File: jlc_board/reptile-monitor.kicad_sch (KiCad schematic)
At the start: 30 parts, among them IC1 ESP32-WROVER-E_M213EH6464PH3Q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, J1 UART, J2 AC_IN, J3 Conn_01x08, J7 LOAD1, J8 LOAD2, K1 ALDP105W, K2 ALDP105W, SW1 RST, SW2 BOOT, U1 NUD3105DMT1G, U3 AP2112K-3.3, Y1 32.768KHz 12.5p

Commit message: rev 2
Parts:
- removed IC1: ESP32-WROVER-E_M213EH6464PH3Q0_, SamacSys_Parts:ESP32WROVEREM213EH6464PH3Q0, symbol SamacSys_Parts:ESP32-WROVER-E_M213EH6464PH3Q0_
- removed J3: Conn_01x08, Connector_PinHeader_2.54mm:PinHeader_2x06_P2.54mm_Vertical, symbol Connector_Generic:Conn_02x06_Odd_Even
- added FB1: 360 m, Capacitor_SMD:C_0805_2012Metric, symbol Device:FerriteBead_Small
- added J1: 1-WIRE, Connector_JST:JST_SH_SM03B-SRSS-TB_1x03-1MP_P1.00mm_Horizontal, symbol Connector:Conn_01x03_Male
- added J8: I2C, Connector_JST:JST_SH_SM04B-SRSS-TB_1x04-1MP_P1.00mm_Horizontal, symbol Connector:Conn_01x04_Male
- added MD1: ESP32-WROVER-E, reptile-monitor:Espressif_Systems-ESP32-WROVER-0-0-MFG, symbol Reptile_Monitor:ESP32-WROVER-E
- added R5, R6, R7: 4.7k, Resistor_SMD:R_0603_1608Metric, symbol Device:R_Small
- U1: renamed from U3; value AP2112K-3.3 -> AP2112M-3.3
- renumbered C9 to C3, C7 to C4, C8 to C5, C10 to C6, D2 to D1, D1 to D2, J1 to J2, J2 to J3, J7 to J4, J8 to J5, R12 to R1, R13 to R2, R1 to R3, R8 to R4, U1 to U2
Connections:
- net +3V3: now also J1.3 (Pin_3), J8.1 (Pin_1), MD1.2 (VDD33), R5.1, R6.1, R7.1
- net +5V: now also FB1.1; no longer C1.1, R1.2, U1.8 (VIN)
- net EN: now also MD1.3 (EN)
- net GND: now also J1.1 (Pin_1), J8.4 (Pin_4), MD1.1 (GND), MD1.15 (GND), MD1.38 (GND), MD1.39 (GND)
- net IO0: now also MD1.25 (IO0)
- net IO18: now also MD1.30 (IO18)
- net IO19: now also MD1.31 (IO19)
- net IO21: now also MD1.33 (IO21)
- net IO22: now also MD1.36 (IO22)
- net IO23: now also MD1.37 (IO23)
- net IO25: now also J8.3 (Pin_3), MD1.10 (IO25), R5.2
- net IO26: now also J8.2 (Pin_2), MD1.11 (IO26), R6.2
- net IO27: now also J1.2 (Pin_2), MD1.12 (IO27), R7.2
- net IO36: now also MD1.4 (IO36)
- net IO39: now also MD1.5 (IO39)
- net IO5: now also MD1.29 (IO5)
- net RXD0: now also MD1.34 (RXD0)
- net TXD0: now also MD1.35 (TXD0)
- net at CL1.1, Y1.2: now also MD1.8 (IO32)
- net at CL2.1, Y1.1: now also MD1.9 (IO33)
- net IO12 renamed MISO
- net MISO: now also MD1.14 (IO12)
- net IO13 renamed LED
- net LED: now also MD1.24 (IO2)
- net IO14 renamed SCLK
- net SCLK: now also MD1.13 (IO14)
- new net: C1.1, FB1.2, R1.2, U1.8 (VIN)
- new net CS0: MD1.23 (IO15)
- new net IO34: MD1.6 (IO34)
- new net IO35: MD1.7 (IO35)
- new net IO4: MD1.26 (IO4)
- new net MOSI: MD1.16 (IO13)
- no-connect marks 10 -> 3
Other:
- note added: "Connectors"
- note removed: "IO Pin Headers"
- moved on the sheet: C4, C5, CL1, CL2, D2, J2, R4, Y1

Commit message: Rev2 - Waffle & Wesley
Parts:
- removed J3: AC_IN, reptile-monitor:Molex-43650-0215-0-0-MFG, symbol Reptile_Monitor:43650-0215
- removed J4: LOAD1, reptile-monitor:Molex-43650-0215-0-0-MFG, symbol Reptile_Monitor:43650-0215
- removed J5: LOAD2, reptile-monitor:Molex-43650-0215-0-0-MFG, symbol Reptile_Monitor:43650-0215
- added J3: AC_IN, SamacSys_Parts:128340212, symbol Connector:Screw_Terminal_01x02
- added J4: LOAD_1, SamacSys_Parts:128340212, symbol Connector:Screw_Terminal_01x02
- added J5: LOAD_2, SamacSys_Parts:128340212, symbol Connector:Screw_Terminal_01x02
- added J6: I/O, Connector_PinHeader_1.27mm:PinHeader_2x05_P1.27mm_Vertical_SMD, symbol Connector_Generic:Conn_02x05_Odd_Even
- C1, C2: footprint Capacitor_SMD:C_0805_2012Metric -> Capacitor_SMD:C_0603_1608Metric
- FB1: footprint Capacitor_SMD:C_0805_2012Metric -> Inductor_SMD:L_0805_2012Metric
- SW1: value RST -> RESET
- renumbered R6 to R5, R5 to R6
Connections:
- net +3V3: now also J6.1 (Pin_1), J6.10 (Pin_10)
- net AC_L: now also F1.2, J3.1 (Pin_1); no longer F1.1
- net AC_N: now also J3.2 (Pin_2), J4.1 (Pin_1), J5.1 (Pin_1)
- net CS0: now also J6.8 (Pin_8)
- net FUSED_AC_L: now also F1.1; no longer F1.2
- net GND: now also J6.9 (Pin_9)
- net IO25: now also J6.7 (Pin_7); no longer J8.3 (Pin_3), R6.2
- net IO26: now also J6.5 (Pin_5); no longer J8.2 (Pin_2), R5.2
- net IO27: now also J6.3 (Pin_3); no longer J1.2 (Pin_2), R7.2
- net LOAD1: now also J4.2 (Pin_2)
- net LOAD2: now also J5.2 (Pin_2)
- net IO0 renamed BOOT
- net IO18 renamed 1-WIRE
- net 1-WIRE: now also J1.2 (Pin_2), R7.2
- net IO19 renamed L1
- net L1: now also U2.2 (1_Gate)
- net IO21 renamed L2
- net L2: now also U2.5 (2_Gate)
- net IO34: no longer names the net of MD1.6 (IO34)
- net IO35: no longer names the net of MD1.7 (IO35)
- net IO4 renamed SCL
- net SCL: now also J8.3 (Pin_3), R6.2
- net IO5 renamed SDA
- net SDA: now also J8.2 (Pin_2), R5.2
- net MISO renamed SDI
- net SDI: now also J6.2 (Pin_2); no longer U2.5 (2_Gate)
- net MOSI renamed SDO
- net SDO: now also J6.4 (Pin_4)
- net SCLK renamed SCK
- net SCK: now also J6.6 (Pin_6); no longer U2.2 (1_Gate)
- no-connect marks 3 -> 7
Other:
- moved on the sheet: C1, C2, D1, F1, FB1, J1, J2, J8, PS1, R1, R2, R5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

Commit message: Revision 3
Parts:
- removed CL1, CL2: 20p, Capacitor_SMD:C_0603_1608Metric, symbol Device:C_Small
- removed SW1: RESET, reptile-monitor:Omron-B3U-1000P-MFG, symbol Reptile_Monitor:B3U-1000P
- removed SW2: BOOT, reptile-monitor:Omron-B3U-1000P-MFG, symbol Reptile_Monitor:B3U-1000P
- removed Y1: 32.768KHz 12.5p, reptile-monitor:Crystal_SMD_3215-2Pin_3.2x1.5mm, symbol Device:Crystal_Small
- added C7: 100n, Capacitor_SMD:C_0603_1608Metric, symbol Device:C_Small
- added D3: Schottky, Diode_SMD:D_SOD-523, symbol Device:D_Schottky_Small
- added SW1: RESET, reptile-monitor:CK-KMR221GLFS-MFG, symbol Reptile_Monitor:KMR221GLFS
- added SW2: BOOT, reptile-monitor:CK-KMR221GLFS-MFG, symbol Reptile_Monitor:KMR221GLFS
- C3, C6: value 0.1u -> 100n
- C4: value 0.1u -> 22u
- C5: value 22u -> 100n
- D1: value LED -> RED
- D2: value LED -> BLUE
- FB1: footprint Inductor_SMD:L_0805_2012Metric -> Inductor_SMD:L_0603_1608Metric_Pad1.05x0.95mm_HandSolder
- R2, R4: value 100r -> 10k
- R3: LCSC (none) -> C22775
- R5, R6, R7: value 4.7k -> 10k
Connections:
- net +3V3: now also R3.2; no longer J2.1 (Pin_1), J6.1 (Pin_1)
- net +5V: now also D3.1 (K)
- net BOOT: now also SW2.1, SW2.2
- net CS0: now also MD1.12 (IO27); no longer MD1.23 (IO15)
- net EN: now also C3.1, C7.1, SW1.1, SW1.2
- net GND: now also D2.1 (K), J2.1 (Pin_1), C7.2, SW1.3, SW1.4, SW1.5 (GROUND), SW2.3, SW2.4, SW2.5 (GROUND); no longer J2.4 (Pin_4), R4.2
- net IO25: now also J6.3 (Pin_3); no longer J6.7 (Pin_7)
- net IO26: now also J6.1 (Pin_1); no longer J6.5 (Pin_5)
- net LED: now also MD1.23 (IO15), R4.2; no longer D2.1 (K), MD1.24 (IO2)
- net RXD0: now also J2.3 (Pin_3); no longer J2.2 (Pin_2)
- net TXD0: now also J2.2 (Pin_2); no longer J2.3 (Pin_3)
- net IO34: now reaches MD1.6 (IO34)
- net IO34: now also J6.7 (Pin_7)
- net IO35: now reaches MD1.7 (IO35)
- net IO35: now also J6.5 (Pin_5)
- net IO22: no longer names the net of MD1.36 (IO22)
- net IO23: no longer names the net of MD1.37 (IO23)
- removed net IO27: J6.3 (Pin_3), MD1.12 (IO27)
- net IO36: no longer names the net of MD1.4 (IO36)
- net IO39: no longer names the net of MD1.5 (IO39)
- new net: D3.2 (A), J2.4 (Pin_4)
- new net IO2: MD1.24 (IO2)
- no-connect marks 7 -> 10
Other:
- moved on the sheet: C4, C5, C6, D2, R4

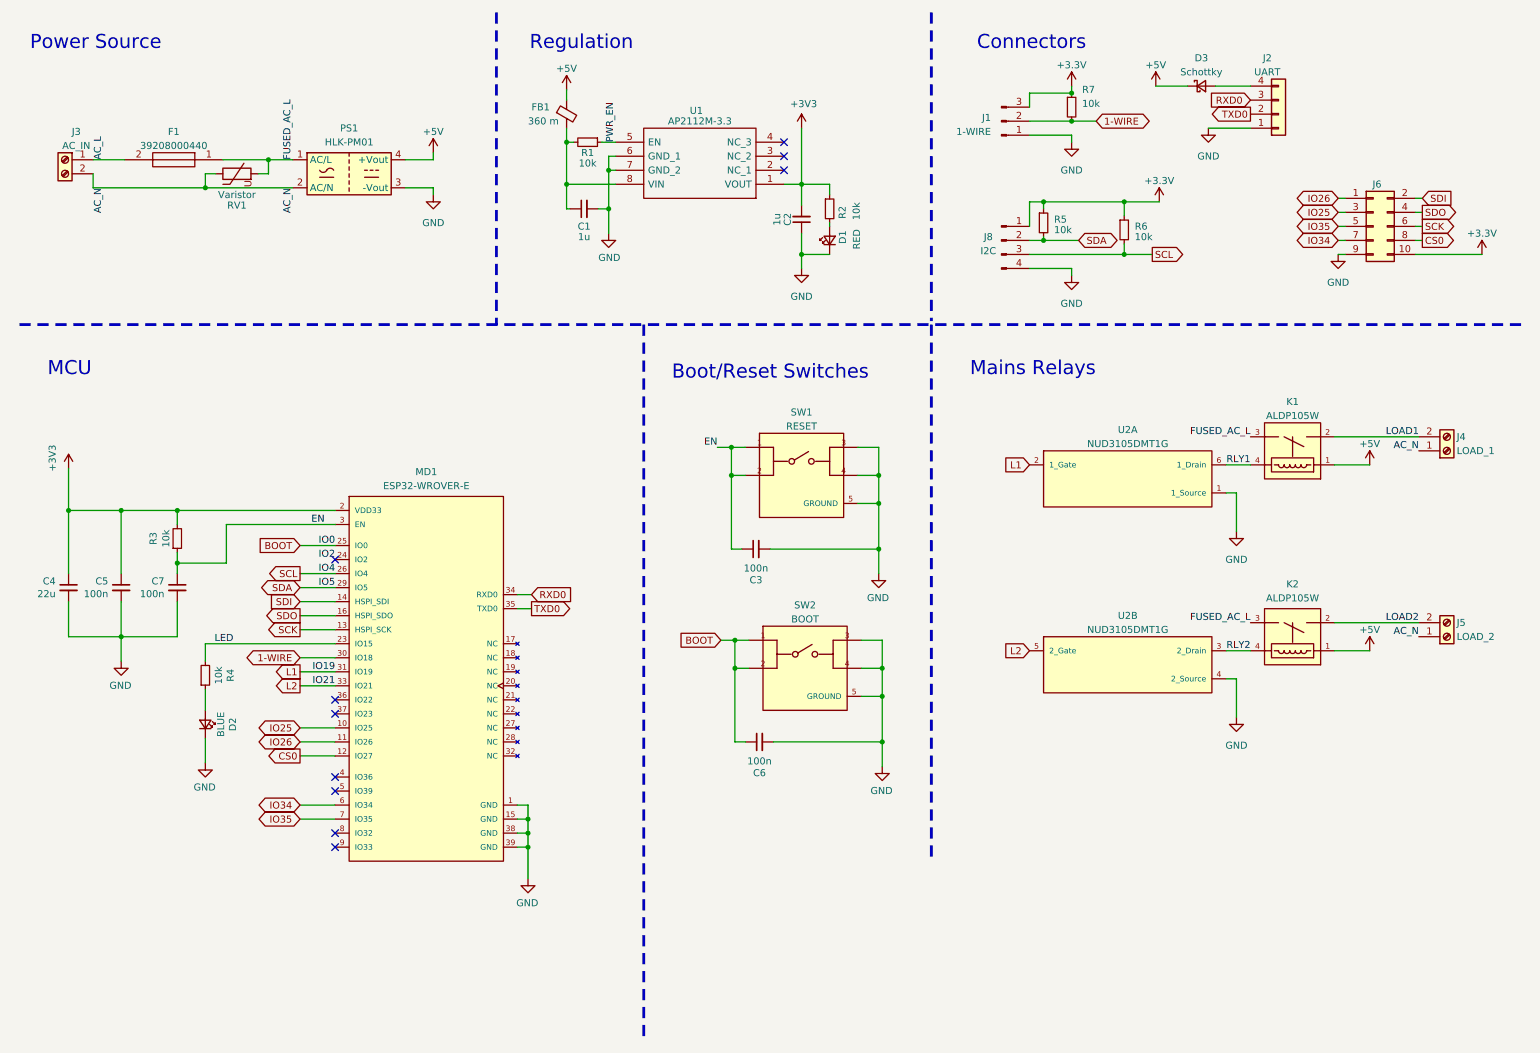
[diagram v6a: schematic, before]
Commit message: separate power board
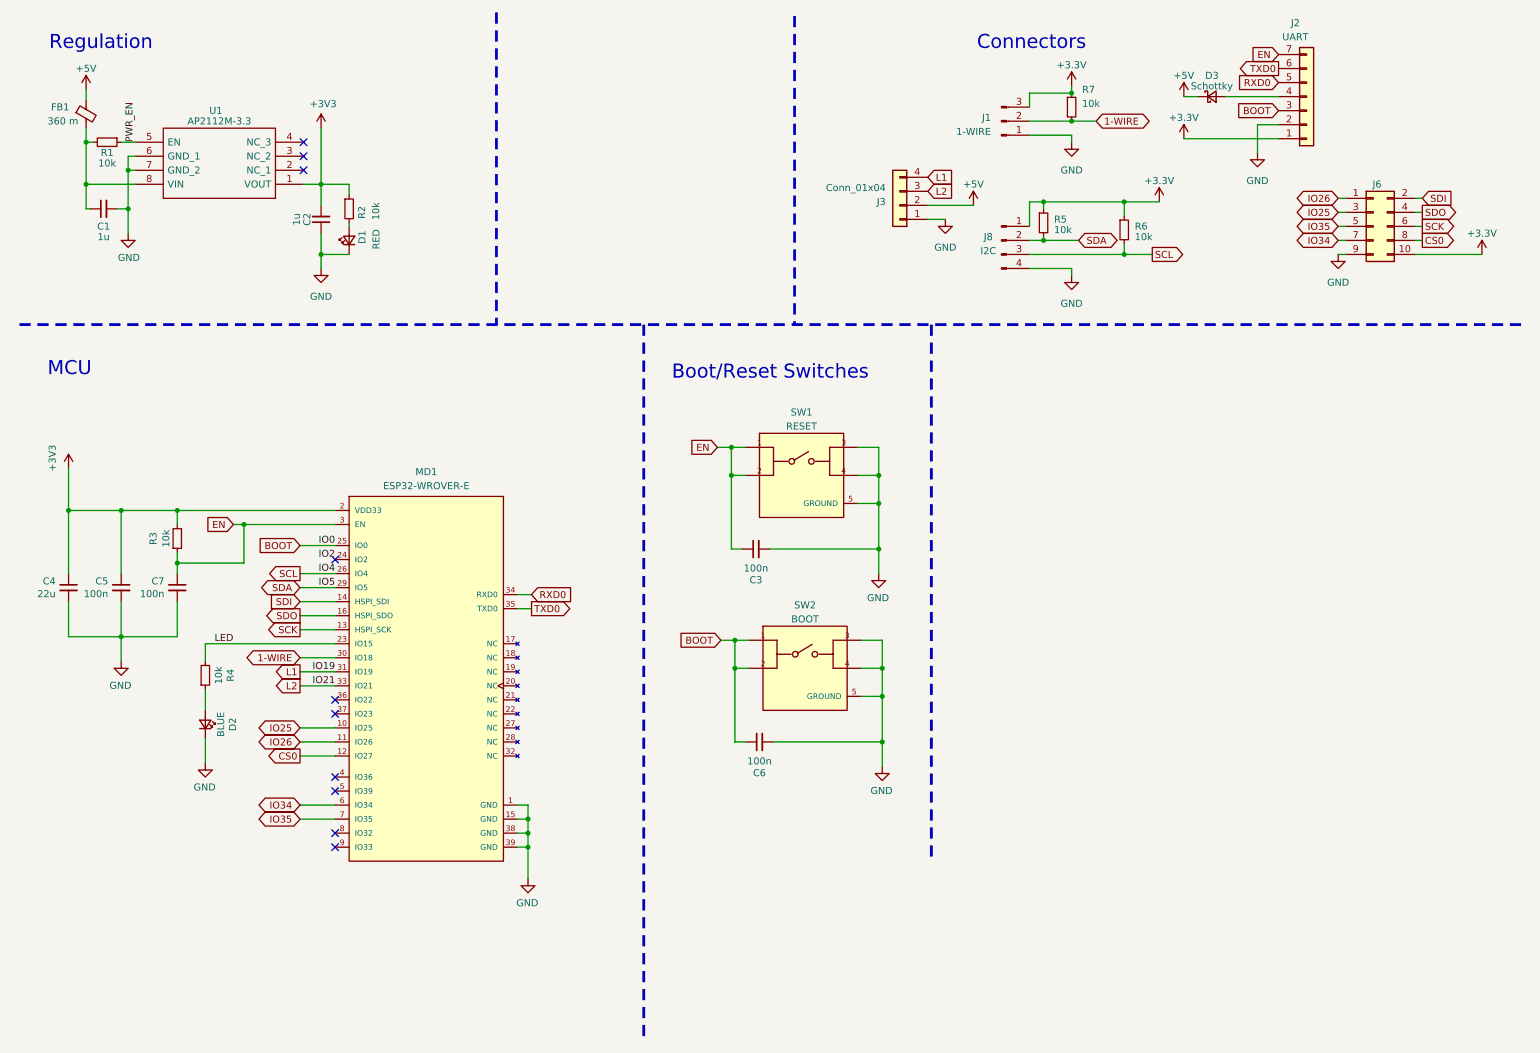
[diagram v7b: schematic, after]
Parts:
- removed F1: 39208000440, SamacSys_Parts:TO508P400X850X850-2P, symbol SamacSys_Parts:39215000000
- removed J3: AC_IN, SamacSys_Parts:128340212, symbol Connector:Screw_Terminal_01x02
- removed J4: LOAD_1, SamacSys_Parts:128340212, symbol Connector:Screw_Terminal_01x02
- removed J5: LOAD_2, SamacSys_Parts:128340212, symbol Connector:Screw_Terminal_01x02
- removed K1, K2: ALDP105W, reptile-monitor:Panasonic-ALDP105W-Manufacturer_Recommended, symbol Reptile_Monitor:ALDP105W
- removed PS1: HLK-PM01, Converter_ACDC:Converter_ACDC_HiLink_HLK-PMxx, symbol Converter_ACDC:HLK-PM01
- removed RV1: Varistor, Varistor:RV_Disc_D7mm_W3.4mm_P5mm, symbol Device:Varistor
- removed U2: NUD3105DMT1G, reptile-monitor:ON_Semi-318F-0-0-0, symbol Reptile_Monitor:NUD3105DMT1G
- added J3: Conn_01x04, Connector_PinSocket_2.54mm:PinSocket_1x04_P2.54mm_Vertical, symbol Connector_Generic:Conn_01x04
- J2: footprint Connector_PinHeader_2.54mm:PinHeader_1x04_P2.54mm_Vertical -> Connector_PinHeader_2.54mm:PinHeader_1x07_P2.54mm_Vertical; symbol Connector_Generic:Conn_01x04 -> Connector_Generic:Conn_01x07
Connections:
- net +3V3: now also J2.1 (Pin_1)
- net +5V: now also J3.2 (Pin_2)
- net BOOT: now also J2.3 (Pin_3)
- net EN: now also J2.7 (Pin_7)
- net GND: now also J2.2 (Pin_2), J3.1 (Pin_1); no longer J2.1 (Pin_1)
- net L1: now also J3.4 (Pin_4)
- net L2: now also J3.3 (Pin_3)
- net RXD0: now also J2.5 (Pin_5); no longer J2.3 (Pin_3)
- net TXD0: now also J2.6 (Pin_6); no longer J2.2 (Pin_2)
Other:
- note removed: "Mains Relays"
- note removed: "Power Source"
- moved on the sheet: C1, C2, D1, D3, FB1, R1, R2, U1

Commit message: Rev 3 - separate power board
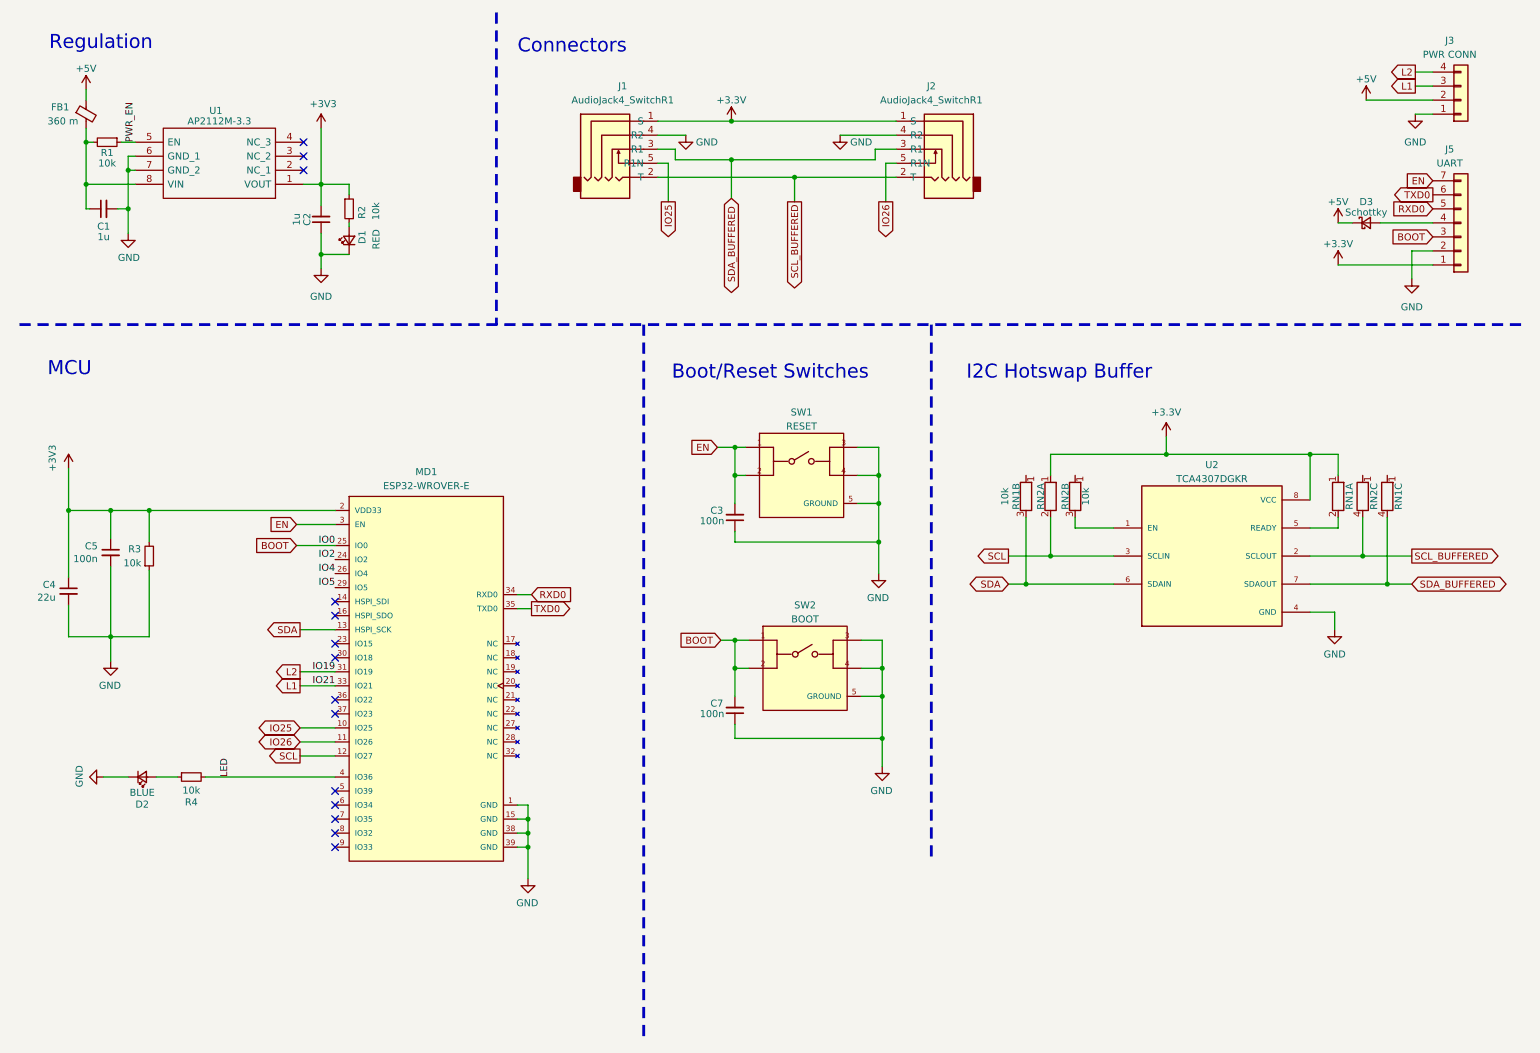
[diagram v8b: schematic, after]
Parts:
- removed C6: 100n, Capacitor_SMD:C_0603_1608Metric, symbol Device:C_Small
- removed J1: 1-WIRE, Connector_JST:JST_SH_SM03B-SRSS-TB_1x03-1MP_P1.00mm_Horizontal, symbol Connector:Conn_01x03_Male
- removed J6: I/O, Connector_PinHeader_1.27mm:PinHeader_2x05_P1.27mm_Vertical_SMD, symbol Connector_Generic:Conn_02x05_Odd_Even
- removed J8: I2C, Connector_JST:JST_SH_SM04B-SRSS-TB_1x04-1MP_P1.00mm_Horizontal, symbol Connector:Conn_01x04_Male
- removed R5, R6, R7: 10k, Resistor_SMD:R_0603_1608Metric, symbol Device:R_Small
- added J1, J2: AudioJack4_SwitchR1, reptile-monitor:Korean Hroparts Elec PJ-227-5A, symbol reptile-monitor:AudioJack4_SwitchR1
- added RN1, RN2: 10k, Resistor_SMD:R_Array_Convex_4x0603, symbol Device:R_Network04_Split
- added U2: TCA4307DGKR, Package_SO:VSSOP-8_3.0x3.0mm_P0.65mm, symbol reptile-monitor:TCA4307DGKR
- J3: value Conn_01x04 -> PWR CONN
- renumbered J2 to J5
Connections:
- net CS0 is gone; now on net SCL: MD1.12 (IO27)
- net SCK is gone; now on net SDA: MD1.13 (IO14)
- net +3V3: now also J1.1 (S), J2.1 (S), RN1.1 (R1.1), RN2.1 (R1.1), U2.8 (VCC)
- net BOOT: now also C7.2
- net EN: now also C3.2; no longer C3.1, C7.1, R3.1
- net GND: now also C3.1, C7.1, R3.1, J1.4 (R2), J2.4 (R2), U2.4 (GND); no longer C3.2, C7.2
- net IO25: now also J1.5 (R1N)
- net IO26: now also J2.5 (R1N)
- net L1: now also J3.3 (Pin_3), MD1.33 (IO21); no longer J3.4 (Pin_4), MD1.31 (IO19)
- net L2: now also J3.4 (Pin_4), MD1.31 (IO19); no longer J3.3 (Pin_3), MD1.33 (IO21)
- net LED: now also MD1.4 (IO36); no longer MD1.23 (IO15)
- net SCL: now also RN2.2 (R1.2), U2.3 (SCLIN); no longer MD1.26 (IO4)
- net SDA: now also RN1.3 (R2.2), U2.6 (SDAIN); no longer MD1.29 (IO5)
- net 1-WIRE: no longer names the net of MD1.30 (IO18)
- net IO34: no longer names the net of MD1.6 (IO34)
- net IO35: no longer names the net of MD1.7 (IO35)
- net SDI: no longer names the net of MD1.14 (IO12)
- net SDO: no longer names the net of MD1.16 (IO13)
- new net: RN2.3 (R2.2), U2.1 (EN)
- new net: RN1.2 (R1.2), U2.5 (READY)
- new net IO4: MD1.26 (IO4)
- new net IO5: MD1.29 (IO5)
- new net SCL_BUFFERED: J1.2 (T), J2.2 (T), RN2.4 (R3.2), U2.2 (SCLOUT)
- new net SDA_BUFFERED: J1.3 (R1), J2.3 (R1), RN1.4 (R3.2), U2.7 (SDAOUT)
- no-connect marks 10 -> 14
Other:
- note added: "I2C Hotswap Buffer"
- moved on the sheet: C4, C5, D2, D3, J3, J5, R3, R4
